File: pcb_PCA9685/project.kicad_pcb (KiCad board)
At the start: 2 copper layers, 18.3 x 25.9 mm, 38 parts, among them IC1 PCA9685PW,118

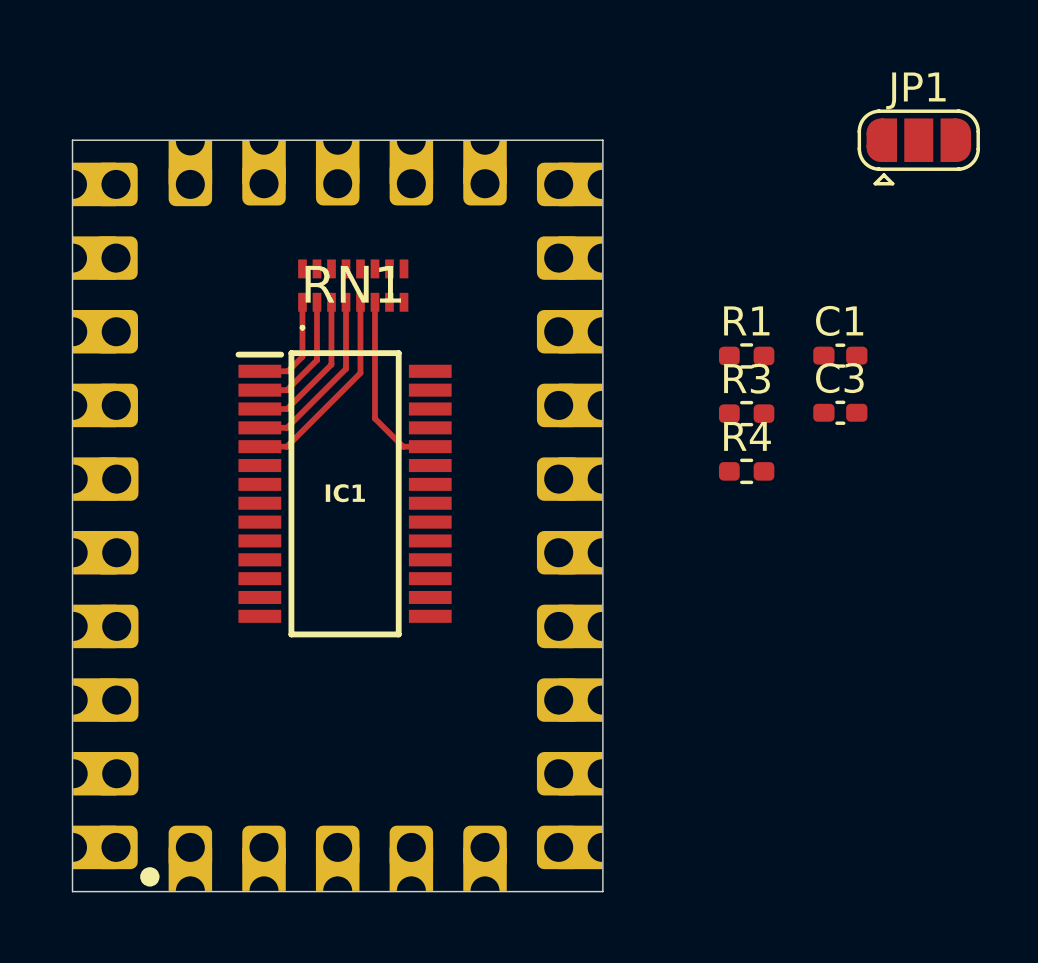
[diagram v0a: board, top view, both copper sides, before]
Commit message: Update PCB for PCA9685
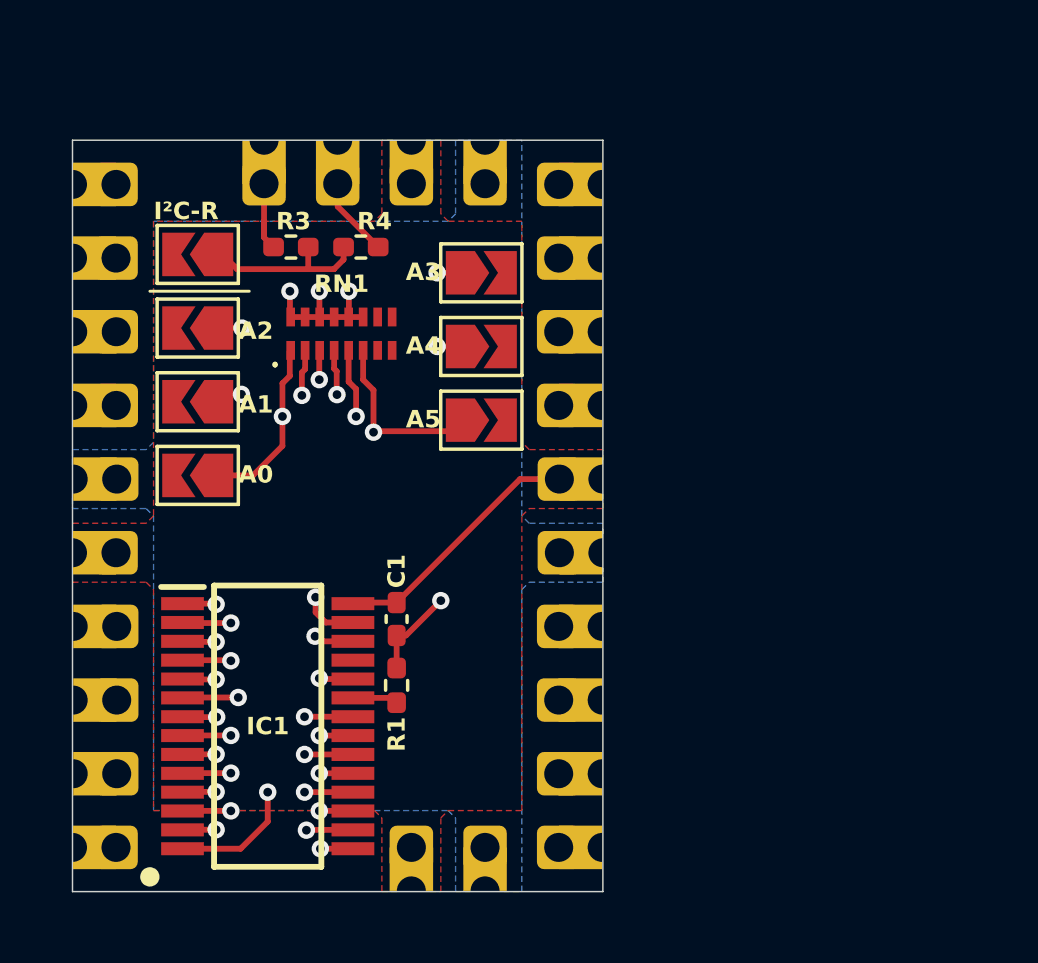
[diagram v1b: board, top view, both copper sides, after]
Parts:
- removed C3: 0.1uF, Capacitor_SMD:C_0402_1005Metric_Pad0.74x0.62mm_HandSolder
- removed J24, J25, J26, J27: ~, Castellated_Holes:Castellated_Hole02
- added JP2: SolderJumper_2_Open, Jumper:SolderJumper-2_P1.3mm_Open_TrianglePad1.0x1.5mm, F.Cu at (100.8, 82.2)
- added JP3: SolderJumper_2_Open, Jumper:SolderJumper-2_P1.3mm_Open_TrianglePad1.0x1.5mm, F.Cu at (100.8, 87.2)
- added JP4: SolderJumper_2_Open, Jumper:SolderJumper-2_P1.3mm_Open_TrianglePad1.0x1.5mm, F.Cu at (100.8, 84.7)
- added JP5: SolderJumper_2_Open, Jumper:SolderJumper-2_P1.3mm_Open_TrianglePad1.0x1.5mm, F.Cu at (110.6, 82.8)
- added JP6: SolderJumper_2_Open, Jumper:SolderJumper-2_P1.3mm_Open_TrianglePad1.0x1.5mm, F.Cu at (110.6, 85.3)
- added JP7: SolderJumper_2_Open, Jumper:SolderJumper-2_P1.3mm_Open_TrianglePad1.0x1.5mm, F.Cu at (110.6, 87.9)
- JP1: value SolderJumper_3_Open -> SolderJumper_2_Open; footprint Jumper:SolderJumper-3_P1.3mm_Open_RoundedPad1.0x1.5mm -> Jumper:SolderJumper-2_P1.3mm_Open_TrianglePad1.0x1.5mm
- moved JP1 27.4 mm to (100.8, 89.8), turned to 180 degrees
- moved J17 18.4 mm to (114.8, 89.9), turned to 180 degrees
- moved J19 18.4 mm to (96.5, 92.5), turned to 0 degrees
- moved C1 17.8 mm to (107.7, 94.7), turned to -90 degrees
- moved R3 16.7 mm to (104.1, 81.9)
- moved R1 16.6 mm to (107.7, 97.0), turned to -90 degrees
- moved R4 15.4 mm to (106.5, 81.9), turned to 180 degrees
- moved IC1 8.44 mm to (103.3, 98.4)
- moved J23 7.62 mm to (108.2, 78.2)
- moved RN1 1.71 mm to (105.8, 84.9)
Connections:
- IC1 pad 25: /OSCIO -> unconnected-(IC1-EXTCLK-Pad25)
- J17 pad 1: /GND -> +3.3V
- J19 pad 1: /A4 -> +3.3V
- J20 pad 1: /A5 -> GNDD
- J23 pad 1: /A2 -> +3.3V
- JP1 pad 1: Net-(JP1-A) -> /A0
- R3 pad 2: Net-(JP1-B) -> Net-(JP2-A)
- R4 pad 2: Net-(JP1-A) -> Net-(JP2-A)
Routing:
- net /SCL: track 0.02 -> 25.4 mm, vias 0 -> 1
- net /IO15: track 0.00 -> 24.9 mm, vias 0 -> 1
- net /IO14: track 0.00 -> 21.9 mm, vias 0 -> 1
- net /SDA: track 0.00 -> 21.6 mm, vias 0 -> 1
- net /IO0: track 0.53 -> 21.9 mm, vias 0 -> 1
- net /IO13: track 0.00 -> 21.0 mm, vias 0 -> 1
- net /IO1: track 0.00 -> 18.5 mm, vias 0 -> 1
- net /IO12: track 0.00 -> 18.0 mm, vias 0 -> 1
- net /IO2: track 0.00 -> 17.6 mm, vias 0 -> 1
- net /A3: track 6.15 -> 21.4 mm, vias 0 -> 3
- net /IO3: track 2.02 -> 16.7 mm, vias 0 -> 1
- net /A4: track 6.96 -> 20.5 mm, vias 0 -> 3
- net GNDD: track 0.00 -> 13.3 mm, vias 0 -> 5
- net /IO11: track 0.00 -> 12.8 mm, vias 0 -> 1
- net /A2: track 5.25 -> 17.6 mm, vias 0 -> 3
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- added copper zone on F.Cu, net +3.3V
- added copper zone on B.Cu, net GNDD
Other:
- copper layers 2 -> 4
- board text added: "A4"
- board text added: "A5"
- board text added: "I²C-R"
- board text removed: "GND1"
- board text removed: "GND2"
- board text removed: "OSCIO"
- board text removed: "VCC1"
- board text removed: "VCC2"

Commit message: Add barcode with the GitHub repository URL on the backsite of the PCBs
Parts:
- added G***: LOGO, LOGO, B.Cu at (105.8, 89.7)

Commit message: Replace QRCode with better version
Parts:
- removed G***: LOGO, LOGO
- added QR*****: https://github.com/fanningert/kicad_pcb_ioexpander, https://github.com/fanningert/kicad_pcb_ioexpander, B.Cu at (105.6, 90.9)

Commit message: Remove connector on own side
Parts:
- removed J21, J22: ~, Castellated_Holes:Castellated_Hole02

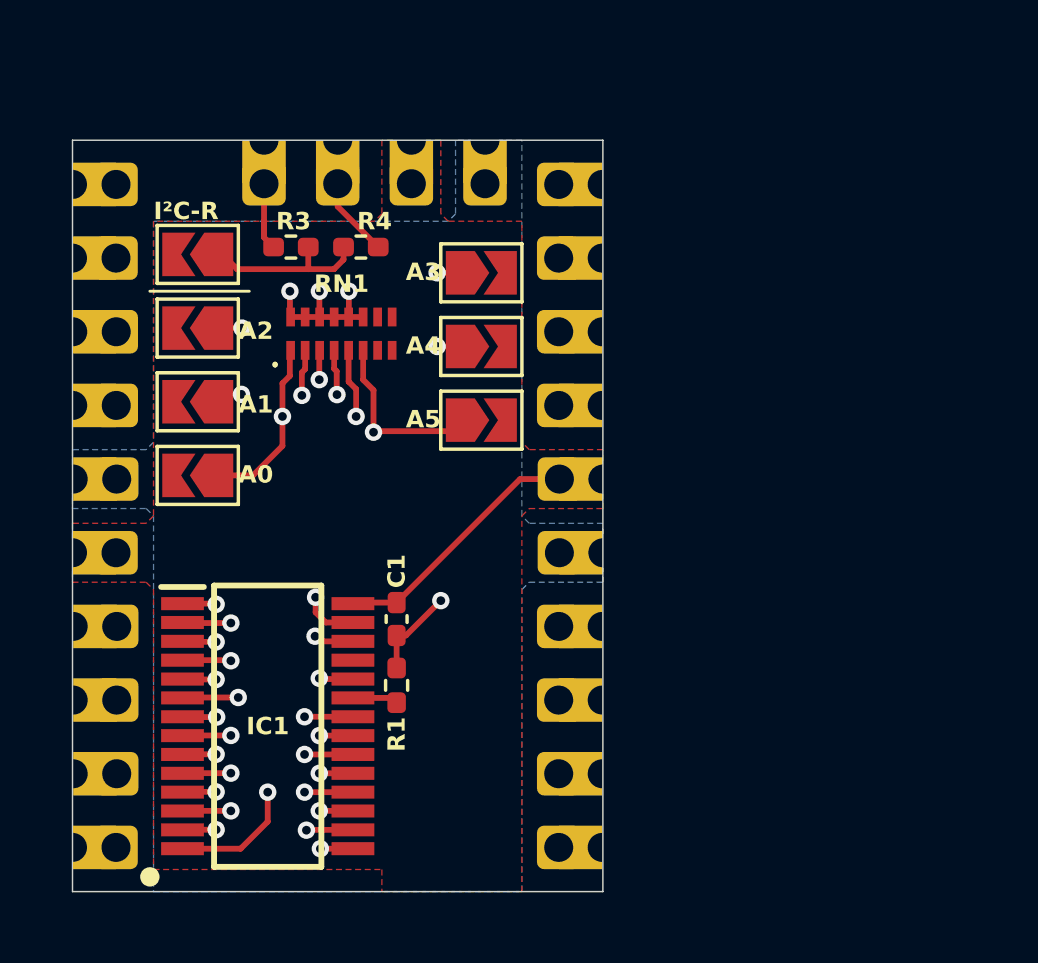
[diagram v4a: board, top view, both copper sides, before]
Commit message: Replace resistor array throw single resistor for reducing vias dn easy component selection
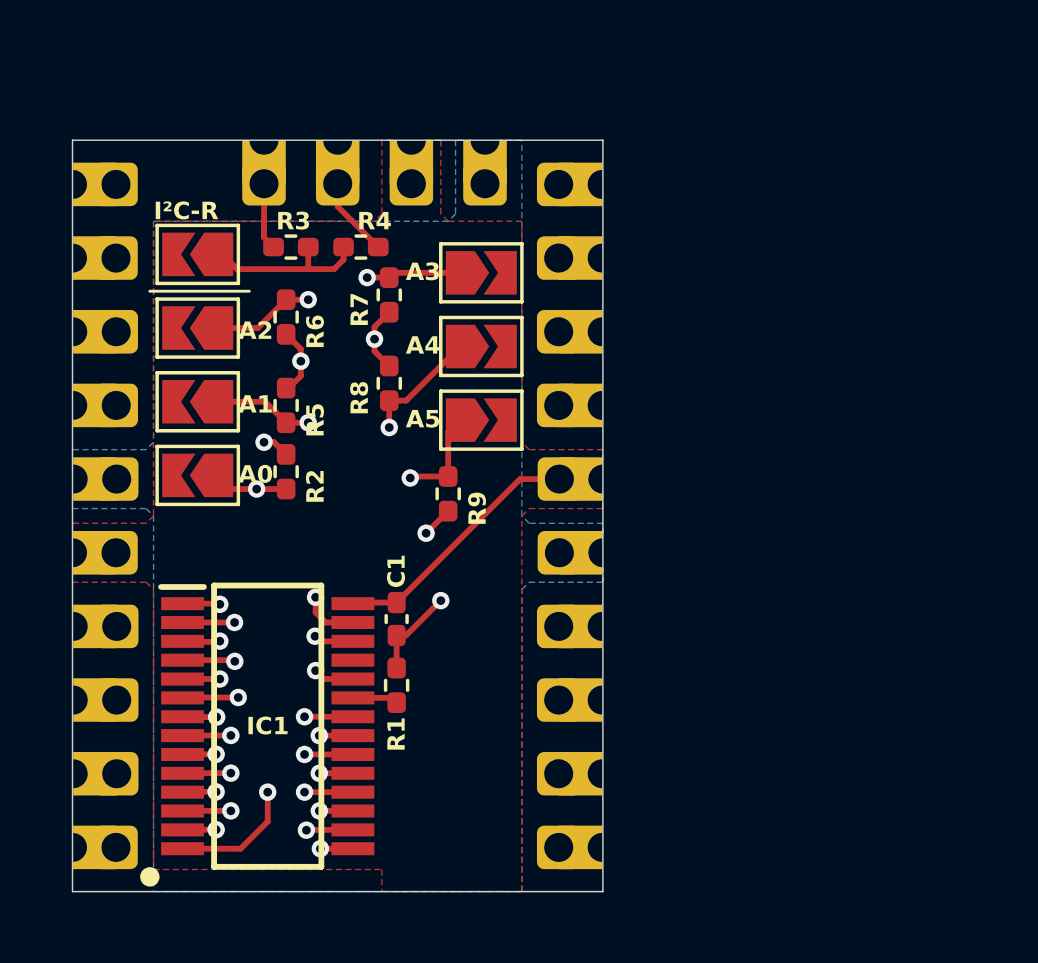
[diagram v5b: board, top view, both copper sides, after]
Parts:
- removed RN1: YC248-JR-0710KL, library:YC248JR0710KL
- added R2: 10k, Resistor_SMD:R_0402_1005Metric_Pad0.72x0.64mm_HandSolder, F.Cu at (103.9, 89.7)
- added R5: 10k, Resistor_SMD:R_0402_1005Metric_Pad0.72x0.64mm_HandSolder, F.Cu at (103.9, 87.4)
- added R6: 10k, Resistor_SMD:R_0402_1005Metric_Pad0.72x0.64mm_HandSolder, F.Cu at (103.9, 84.3)
- added R7: 10k, Resistor_SMD:R_0402_1005Metric_Pad0.72x0.64mm_HandSolder, F.Cu at (107.4, 83.6)
- added R8: 10k, Resistor_SMD:R_0402_1005Metric_Pad0.72x0.64mm_HandSolder, F.Cu at (107.4, 86.6)
- added R9: 10k, Resistor_SMD:R_0402_1005Metric_Pad0.72x0.64mm_HandSolder, F.Cu at (109.5, 90.4)
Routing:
- net /A0: track 14.5 -> 8.46 mm
- net /A5: track 17.2 -> 13.4 mm
- net /A4: track 20.5 -> 17.1 mm, vias 3 -> 2
- net /A1: track 15.4 -> 13.1 mm, vias 3 -> 2
- net /A2: track 17.6 -> 19.6 mm, vias 3 -> 2
- net GNDD: track 13.3 -> 14.8 mm, vias 5 -> 6
- net /A3: track 21.4 -> 20.6 mm, vias 3 -> 2
